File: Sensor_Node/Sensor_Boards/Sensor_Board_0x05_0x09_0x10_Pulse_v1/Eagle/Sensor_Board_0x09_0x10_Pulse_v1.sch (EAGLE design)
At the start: 21 parts, among them J3 1x3 RA Female .1", J4 ARDUINO_ISP, J6 1x3 RA Female .1", U2 ATMEGA328P_TQFP, Y1 8MHZ

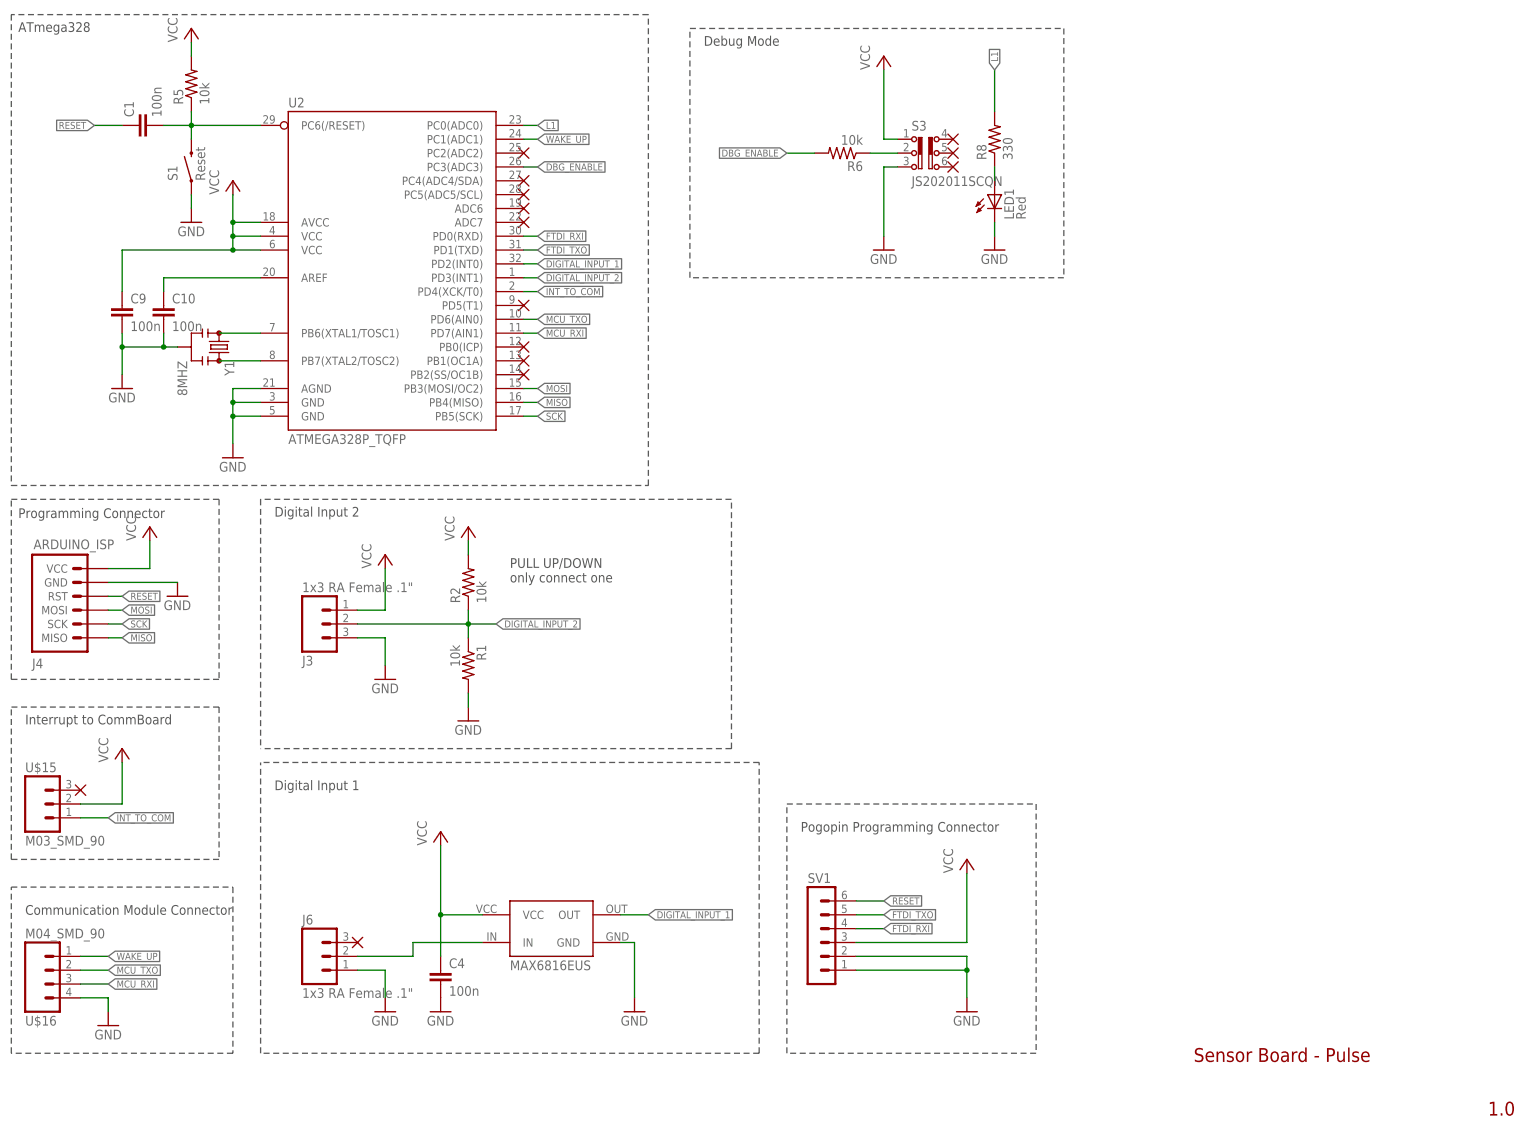
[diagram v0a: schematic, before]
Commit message: Pulse-Board
- Reset path
- Various small things
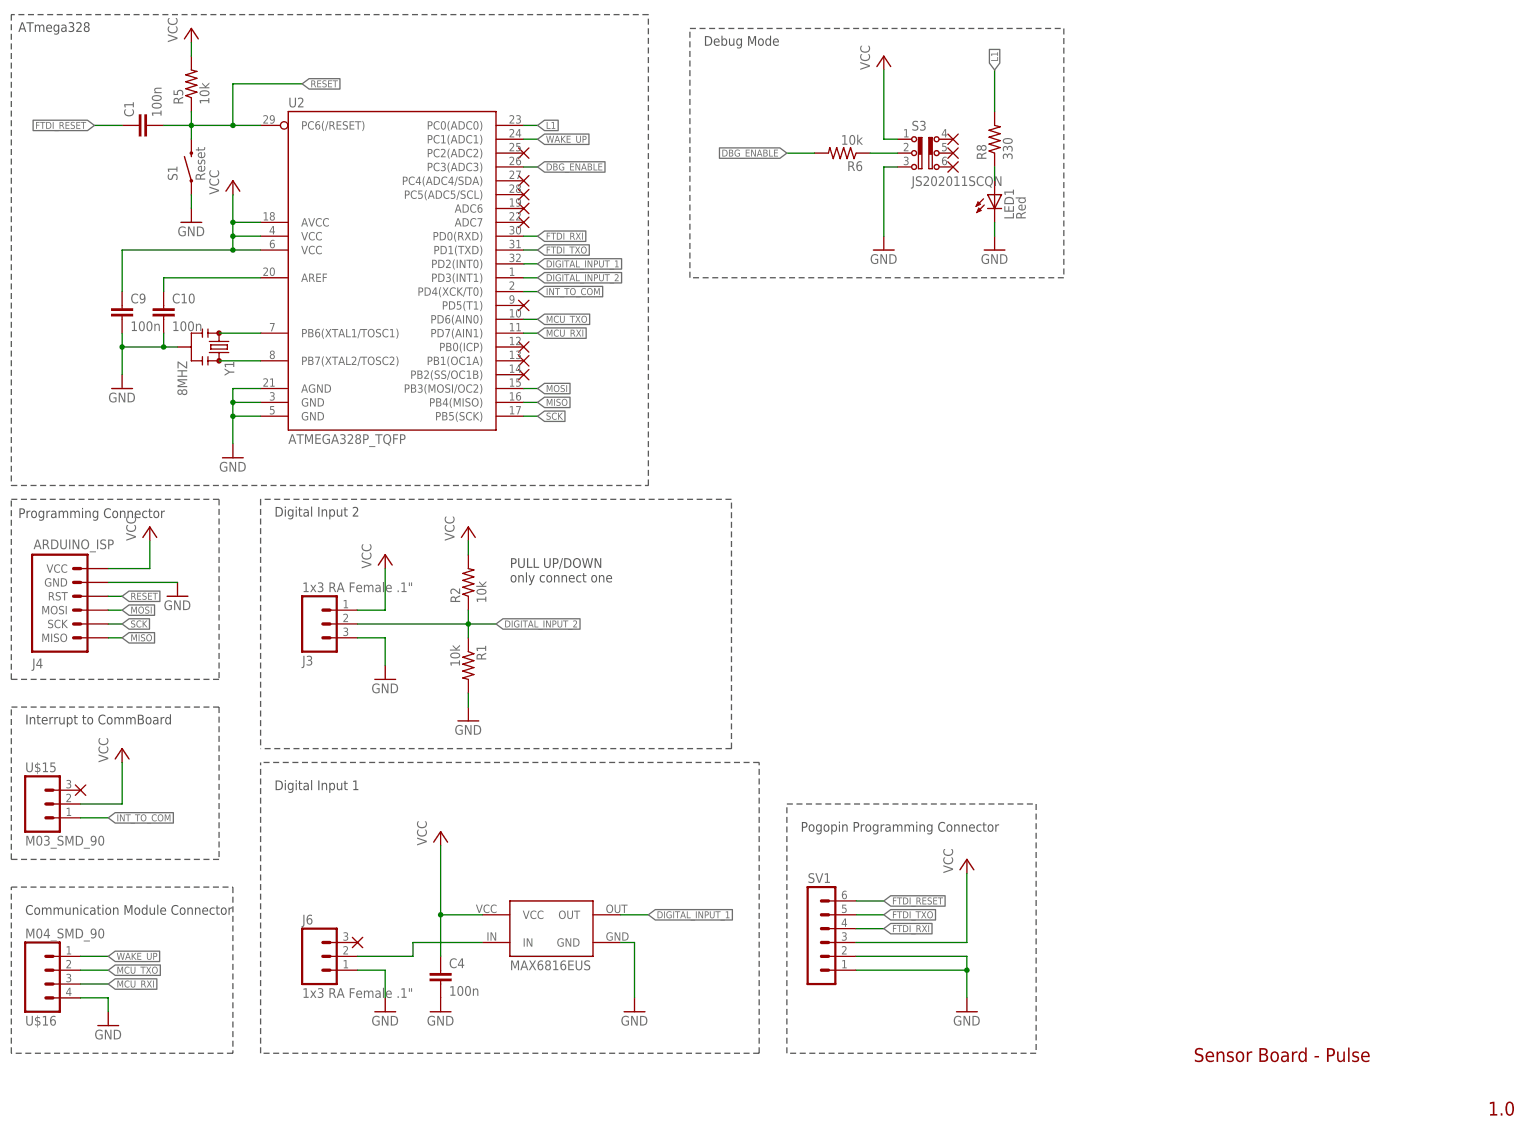
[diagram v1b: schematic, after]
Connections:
- removed net N$5: C1.2, R5.1, S1.RIGHT, U2.PC6(/RESET)
- new net FTDI_RESET: C1.1, SV1.6
- net RESET: now also C1.2, R5.1, S1.RIGHT, U2.PC6(/RESET); no longer C1.1, SV1.6
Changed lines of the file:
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@@
 </segment>
 <segment>
-<pinref part="C1" gate="G$1" pin="1"/>
-<wire x1="27.94" y1="182.88" x2="22.86" y2="182.88" width="0.1524" layer="91"/>
-<label x="22.86" y="182.88" size="1.27" layer="95" rot="R180" xref="yes"/>
-</segment>
-<segment>
-<pinref part="SV1" gate="1" pin="6"/>
-<wire x1="162.56" y1="40.64" x2="167.64" y2="40.64" width="0.1524" layer="91"/>
-<label x="167.64" y="40.64" size="1.27" layer="95" xref="yes"/>
+<pinref part="C1" gate="G$1" pin="2"/>
+<pinref part="U2" gate="U$1" pin="PC6(/RESET)"/>
+<wire x1="35.56" y1="182.88" x2="40.64" y2="182.88" width="0.1524" layer="91"/>
+<pinref part="R5" gate="G$1" pin="1"/>
+<wire x1="40.64" y1="182.88" x2="48.26" y2="182.88" width="0.1524" layer="91"/>
+<wire x1="48.26" y1="182.88" x2="53.34" y2="182.88" width="0.1524" layer="91"/>
+<wire x1="40.64" y1="185.42" x2="40.64" y2="182.88" width="0.1524" layer="91"/>
+<junction x="40.64" y="182.88"/>
+<pinref part="S1" gate="G$1" pin="RIGHT"/>
+<wire x1="40.64" y1="180.34" x2="40.64" y2="182.88" width="0.1524" layer="91"/>
+<wire x1="48.26" y1="182.88" x2="48.26" y2="190.5" width="0.1524" layer="91"/>
+<junction x="48.26" y="182.88"/>
+<wire x1="48.26" y1="190.5" x2="60.96" y2="190.5" width="0.1524" layer="91"/>
+<label x="60.96" y="190.5" size="1.27" layer="95" xref="yes"/>
 </segment>
 </net>
@@
 </segment>
 </net>
-<net name="N$5" class="0">
-<segment>
-<pinref part="C1" gate="G$1" pin="2"/>
-<pinref part="U2" gate="U$1" pin="PC6(/RESET)"/>
-<wire x1="35.56" y1="182.88" x2="40.64" y2="182.88" width="0.1524" layer="91"/>
-<pinref part="R5" gate="G$1" pin="1"/>
-<wire x1="40.64" y1="182.88" x2="53.34" y2="182.88" width="0.1524" layer="91"/>
-<wire x1="40.64" y1="185.42" x2="40.64" y2="182.88" width="0.1524" layer="91"/>
-<junction x="40.64" y="182.88"/>
-<pinref part="S1" gate="G$1" pin="RIGHT"/>
-<wire x1="40.64" y1="180.34" x2="40.64" y2="182.88" width="0.1524" layer="91"/>
-</segment>
-</net>
 <net name="FTDI_RXI" class="0">
 <segment>
@@
 </segment>
 </net>
+<net name="FTDI_RESET" class="0">
+<segment>
+<pinref part="SV1" gate="1" pin="6"/>
+<wire x1="162.56" y1="40.64" x2="167.64" y2="40.64" width="0.1524" layer="91"/>
+<label x="167.64" y="40.64" size="1.27" layer="95" xref="yes"/>
+</segment>
+<segment>
+<pinref part="C1" gate="G$1" pin="1"/>
+<wire x1="27.94" y1="182.88" x2="22.86" y2="182.88" width="0.1524" layer="91"/>
+<label x="22.86" y="182.88" size="1.27" layer="95" rot="R180" xref="yes"/>
+</segment>
+</net>

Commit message: Changes on PulseBoard
- startet replacement and rerouting
- corrected faulty VCC-Connection
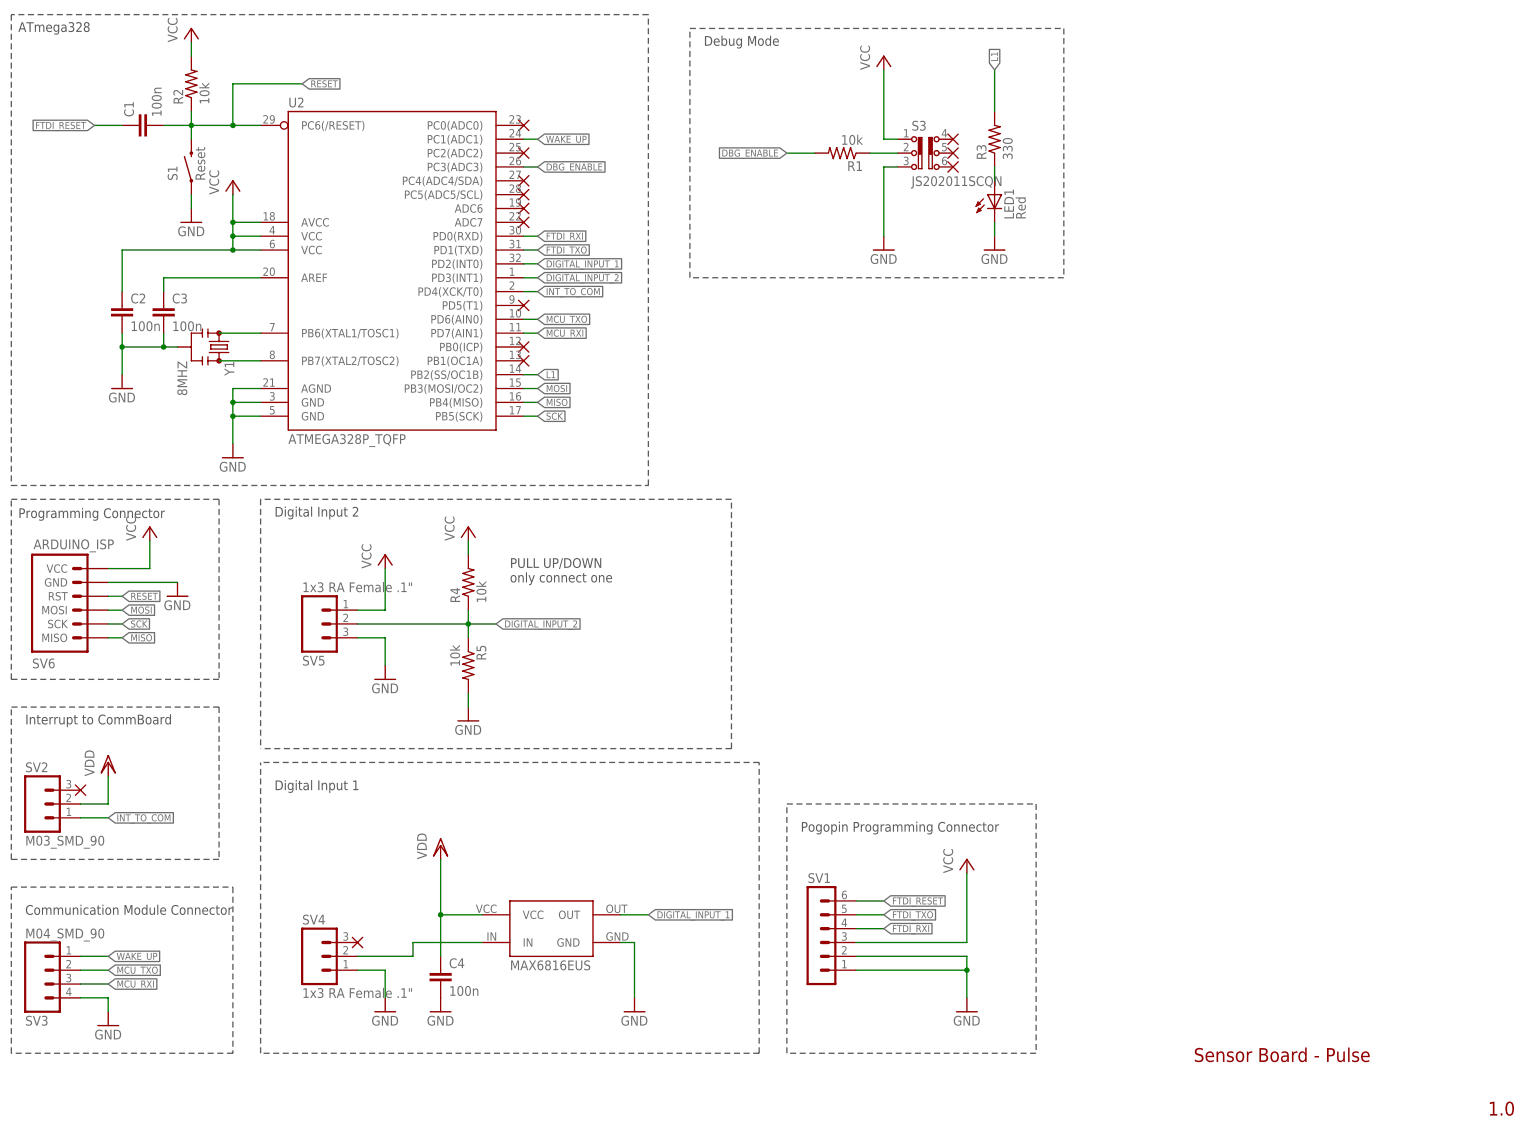
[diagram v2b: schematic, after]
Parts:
- removed R6: 10k, SparkFun-Passives:RESISTOR0805-RES
- added R4: 10k, SparkFun-Passives:RESISTOR0805-RES
- renumbered C10 to C3, C9 to C2, J3 to SV5, J4 to SV6, J6 to SV4, R8 to R3, U$15 to SV2, U$16 to SV3
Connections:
- new net VDD: C4.1, SV2.2, U$2.VCC
- net DBG_ENABLE: now also R1.2; no longer R6.2
- net DIGITAL_INPUT_2: now also R4.1, R5.1; no longer R1.1, R2.1
- net GND: now also R5.2; no longer R1.2
- net L1: now also U2.PB2(SS/OC1B); no longer U2.PC0(ADC0)
- net N$3: now also R1.1; no longer R6.1
- net RESET: now also R2.1; no longer R5.1
- net VCC: now also R4.2; no longer C4.1, R5.2, SV2.2, U$2.VCC
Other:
- moved on the sheet: R1, R2, R5

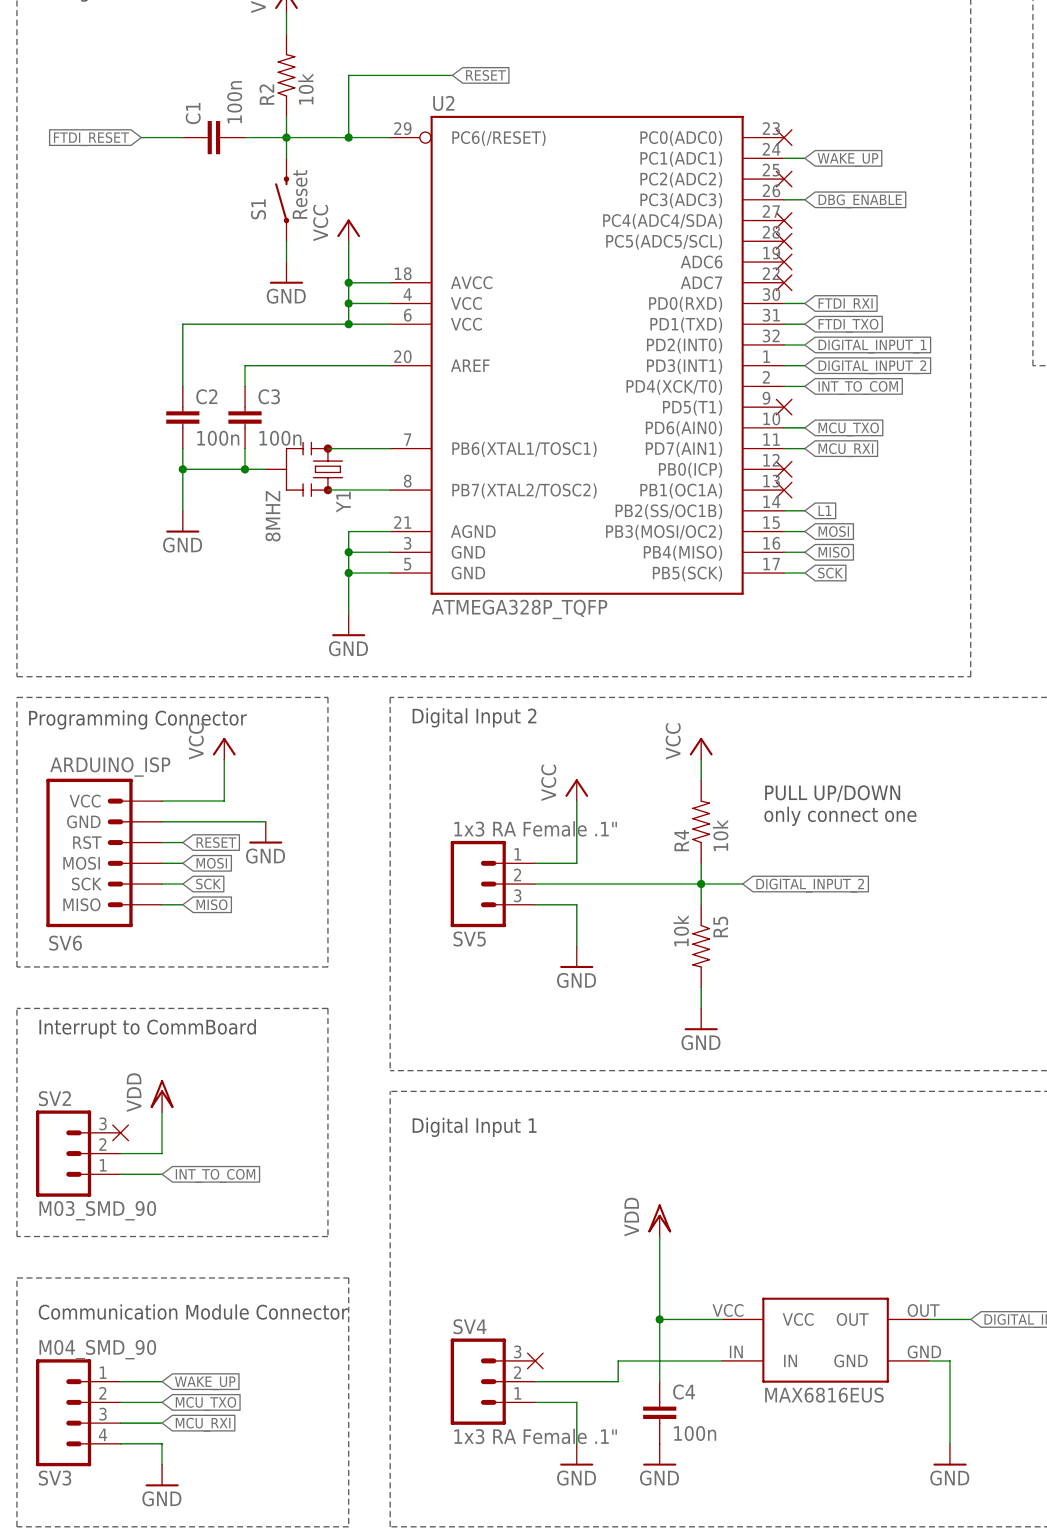
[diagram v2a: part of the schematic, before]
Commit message: Finished Changes on PulseBoard
Pulseboard:
- tidied up routing and placement

TSL2561:
- tidied up some connections
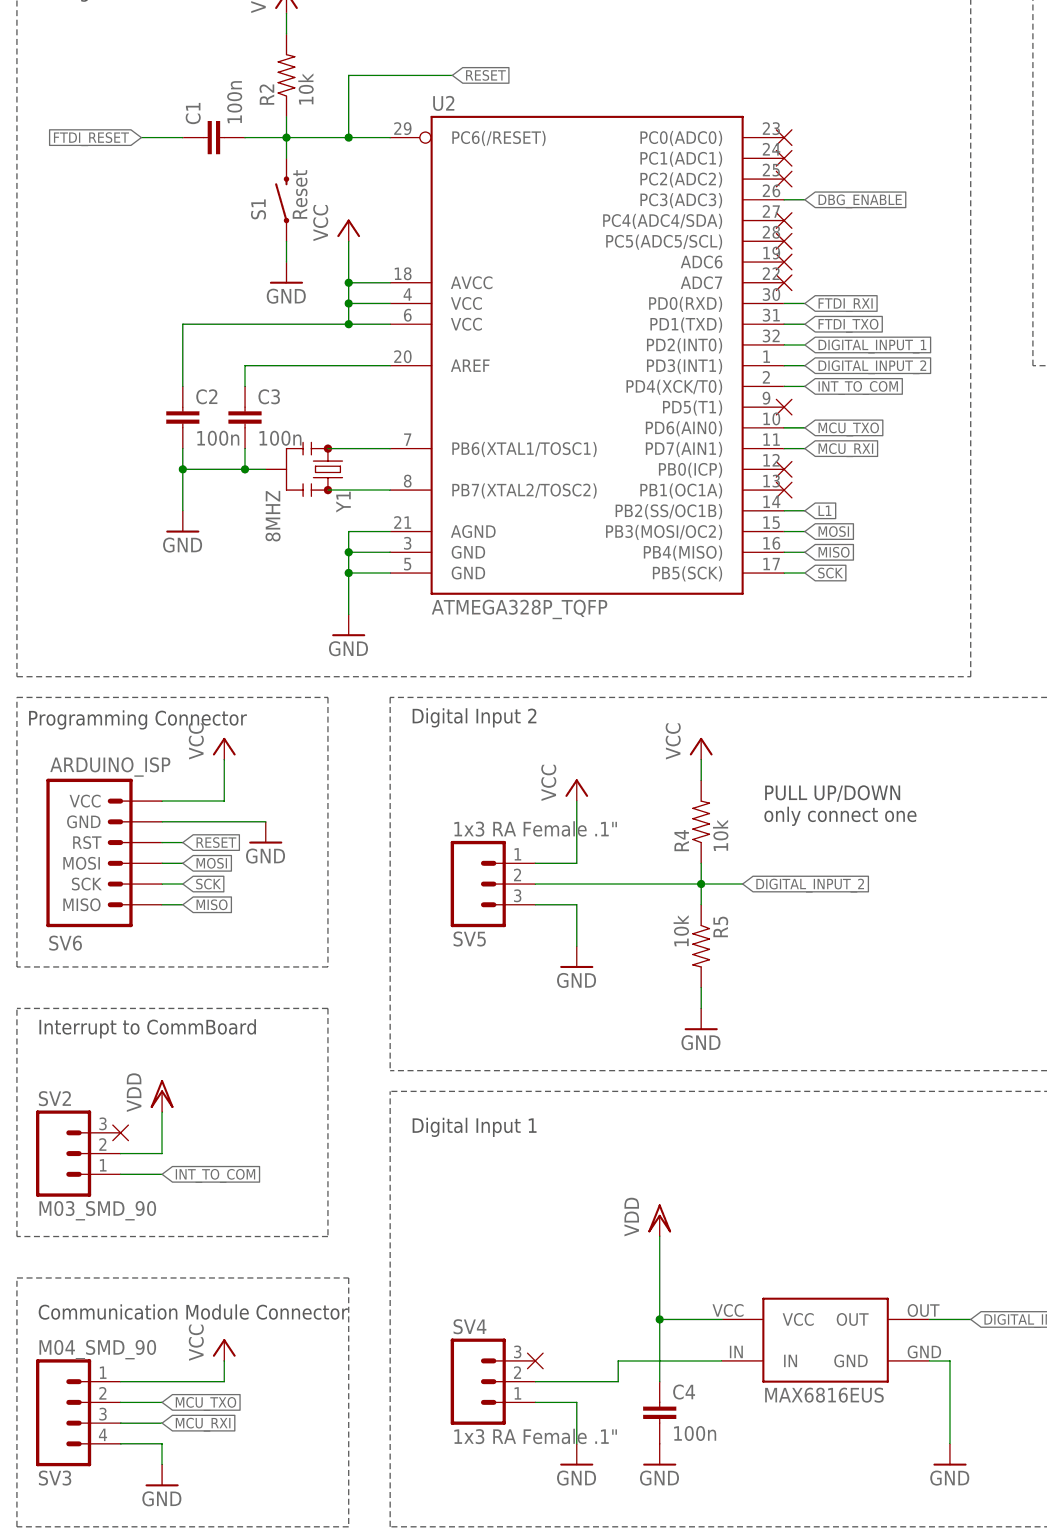
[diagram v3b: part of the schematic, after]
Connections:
- removed net WAKE_UP: SV3.1, U2.PC1(ADC1)
- net VCC: now also SV3.1
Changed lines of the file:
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@@
 <part name="VDD1" library="supply1" library_urn="urn:adsk.eagle:library:371" deviceset="VDD" device=""/>
 <part name="VDD2" library="supply1" library_urn="urn:adsk.eagle:library:371" deviceset="VDD" device=""/>
+<part name="P+5" library="supply1" deviceset="VCC" device=""/>
+<part name="U$8" library="myownthings" deviceset="N/C" device=""/>
 </parts>
 <sheets>
@@
 <instance part="VDD1" gate="G$1" x="25.4" y="66.04"/>
 <instance part="VDD2" gate="G$1" x="86.36" y="50.8"/>
+<instance part="P+5" gate="VCC" x="33.02" y="35.56"/>
+<instance part="U$8" gate="G$1" x="101.6" y="180.34"/>
 </instances>
 <busses>
@@
 <wire x1="182.88" y1="33.02" x2="182.88" y2="45.72" width="0.1524" layer="91"/>
 </segment>
+<segment>
+<pinref part="SV3" gate="G$1" pin="1"/>
+<pinref part="P+5" gate="VCC" pin="VCC"/>
+<wire x1="20.32" y1="30.48" x2="33.02" y2="30.48" width="0.1524" layer="91"/>
+<wire x1="33.02" y1="30.48" x2="33.02" y2="33.02" width="0.1524" layer="91"/>
+</segment>
 </net>
 <net name="RESET" class="0">
@@
 </segment>
 </net>
-<net name="WAKE_UP" class="0">
-<segment>
-<wire x1="20.32" y1="30.48" x2="25.4" y2="30.48" width="0.1524" layer="91"/>
-<label x="25.4" y="30.48" size="1.27" layer="95" xref="yes"/>
-<pinref part="SV3" gate="G$1" pin="1"/>
-</segment>
-<segment>
-<pinref part="U2" gate="U$1" pin="PC1(ADC1)"/>
-<wire x1="101.6" y1="180.34" x2="104.14" y2="180.34" width="0.1524" layer="91"/>
-<label x="104.14" y="180.34" size="1.27" layer="95" xref="yes"/>
-</segment>
-</net>
